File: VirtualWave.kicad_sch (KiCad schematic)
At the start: 13 parts, among them U1 LM358, U2 LM555xM

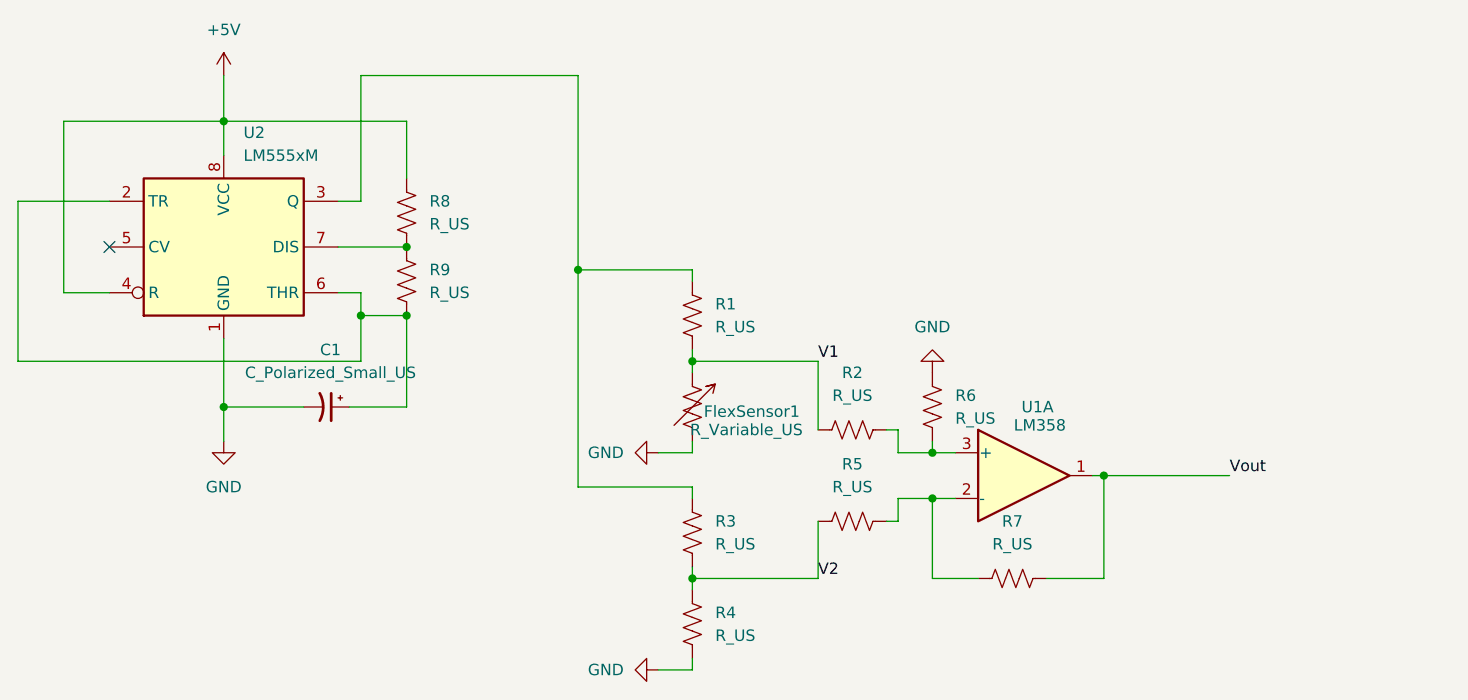
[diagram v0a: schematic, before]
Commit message: voltage inputs of the differential op amp go through voltage followers to maintain voltage
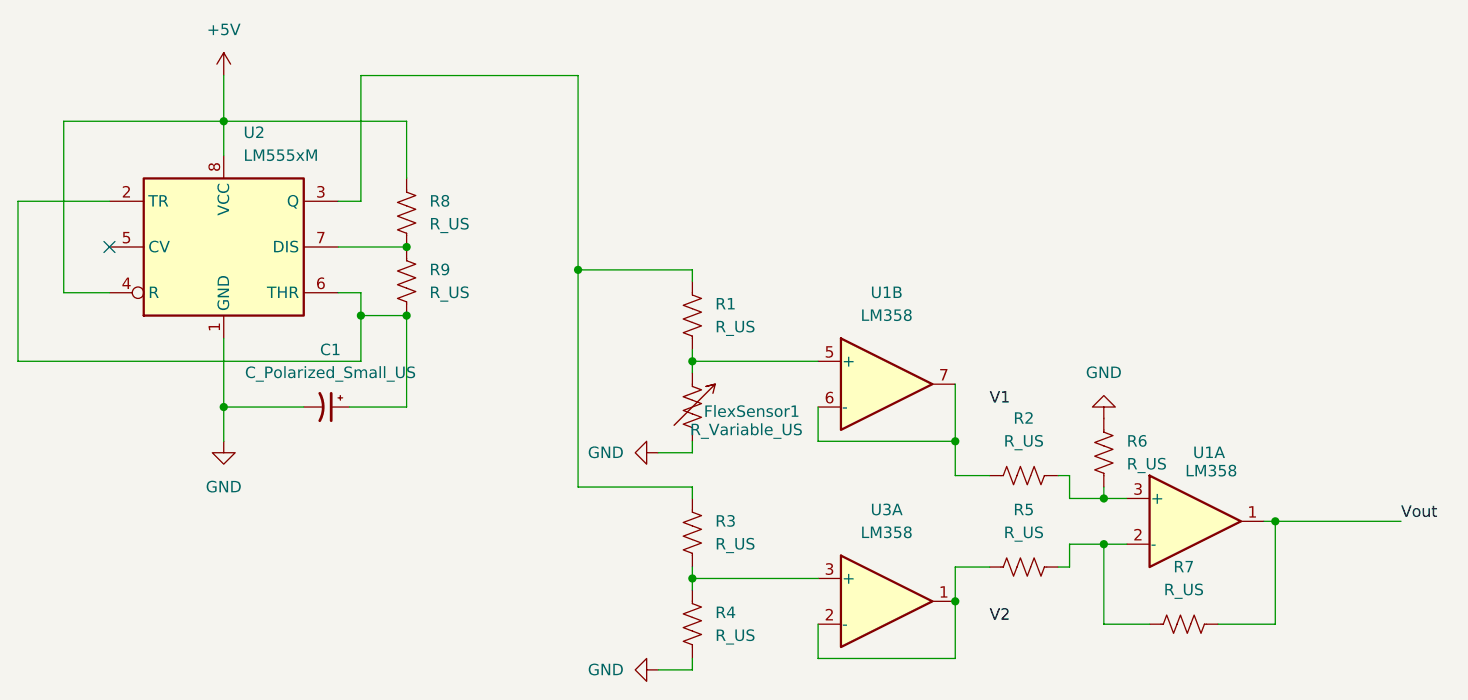
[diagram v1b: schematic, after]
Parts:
- added unit 2 of U1
- added U3: LM358, symbol Amplifier_Operational:LM358
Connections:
- net V1: no longer FlexSensor1.1, R1.2, R2.1
- net V2: no longer R3.2, R4.1, R5.1
- new net: R3.2, R4.1, U3.3 (+)
- new net: R5.1, U3.1, U3.2 (-)
- new net: FlexSensor1.1, R1.2, U1.5 (+)
- new net: R2.1, U1.6 (-), U1.7
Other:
- moved on the sheet: R2, R5, R6, R7, U1A
